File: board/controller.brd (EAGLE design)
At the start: 100 x 100 mm, 61 parts, among them J1 X, J10 COOLANT, J12 VIN, J13 GND, J15 A, J16 +5V, J17 PROBE, J18 FEED_OVERRIDE, J19 MOTOR_CURRENT, J2 Y, J20 WHEEL, J22 DISPLAY, J23 ERROR, J24 HOLDING, J25 SPINDLE, J26 SD_READER, J3 Z, J4 RESET, J5 Z_DISPLAY, J6 FEED_HOLD, J8 CYCLE_START, U5 SENSOR-IR-THRU

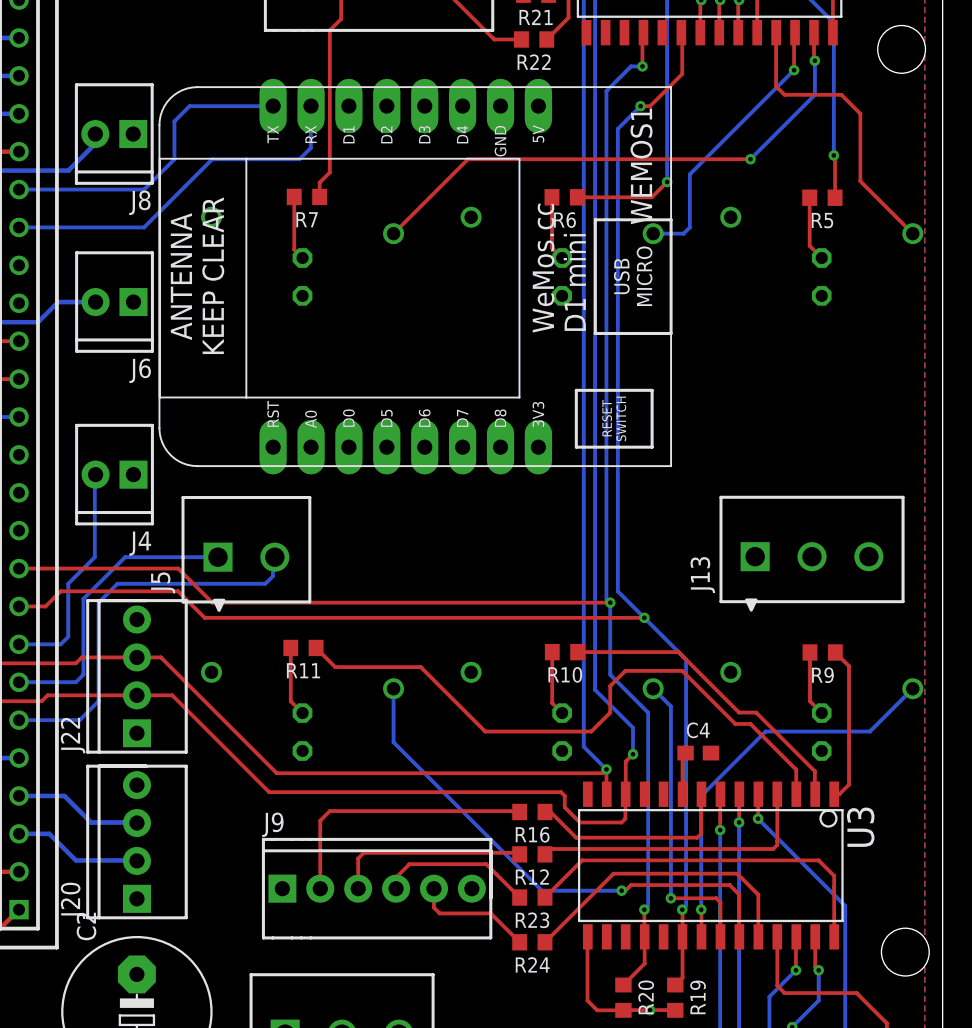
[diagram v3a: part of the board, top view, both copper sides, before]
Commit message: fixed 5V0/GND islands
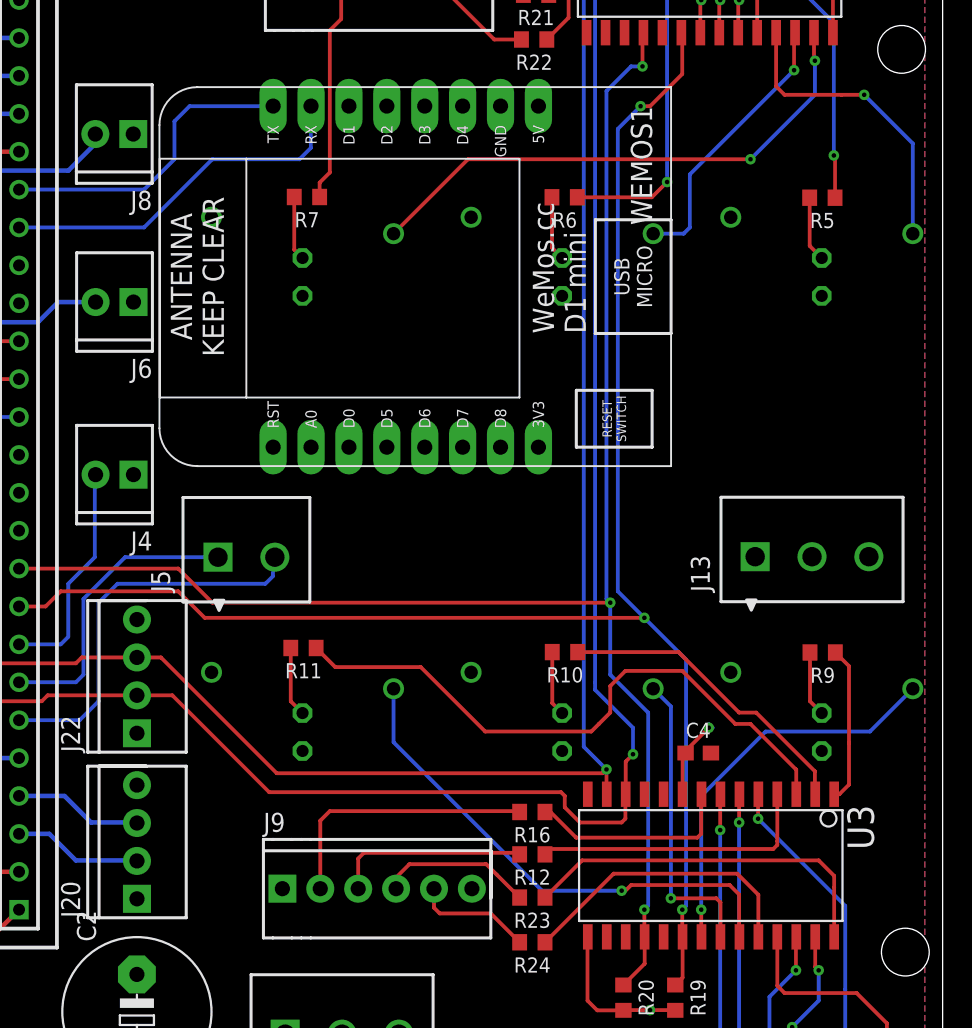
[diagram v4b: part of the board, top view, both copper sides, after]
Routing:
- net 5V0: track 22.3 -> 25.2 mm, vias 3 -> 4
- net S2A1: track 19.5 -> 20.4 mm, vias 0 -> 1
- net RESET_IN: vias 1 -> 0

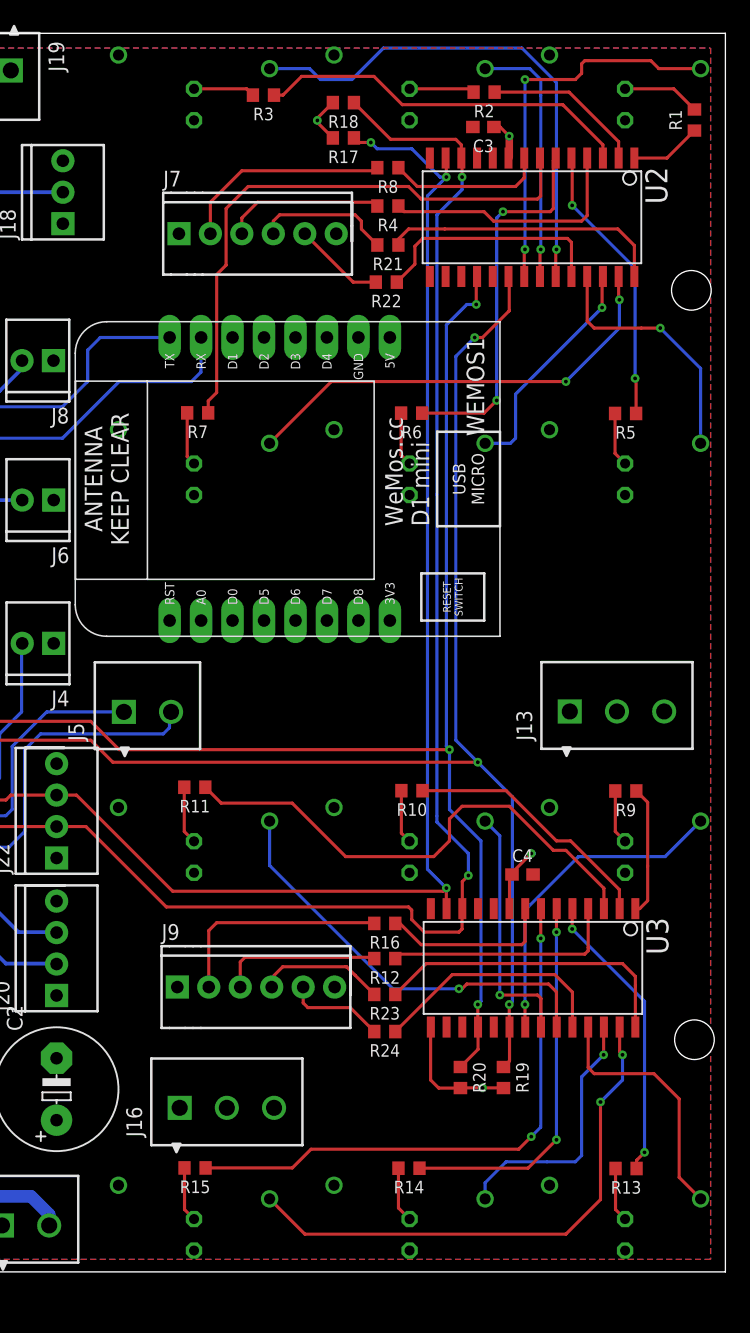
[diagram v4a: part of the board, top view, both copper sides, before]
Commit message: corrected keyboard switch dimensions
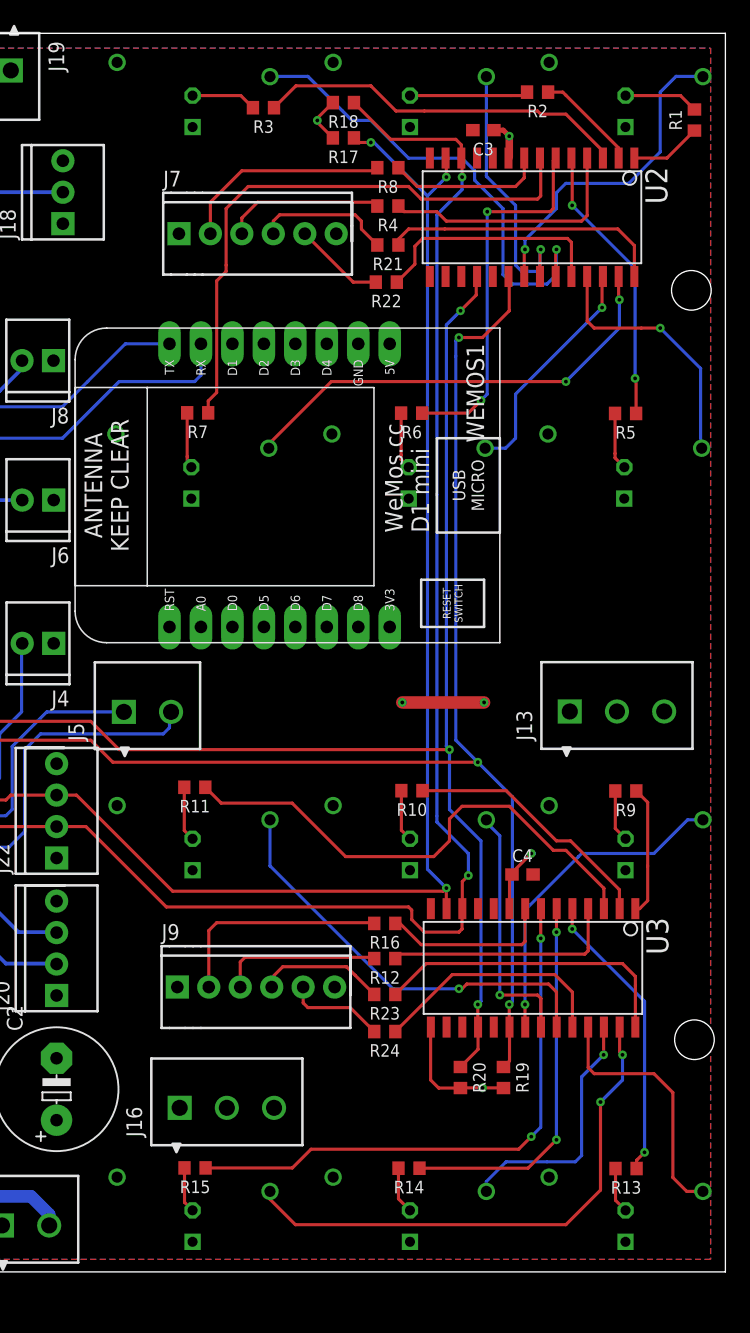
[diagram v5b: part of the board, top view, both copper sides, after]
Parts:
- moved S1 27.7 mm to (100.6, 84.9)
- moved S2 27.5 mm to (100.5, 54.9)
- moved S3 27.5 mm to (100.6, 24.9)
- moved S4 27.3 mm to (100.6, -5.10)
- moved R2 4.32 mm to (84.8, 95.2)
- moved R3 1.02 mm to (62.7, 94.0)
- moved WEMOS1 0.52 mm to (62.7, 62.2)
- moved C3 0.25 mm to (80.5, 92.2)
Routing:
- net 5V0: track 25.2 -> 31.7 mm, vias 4 -> 6
- net S1A1: track 31.4 -> 26.4 mm, vias 2 -> 1
- net N$2: track 13.0 -> 8.37 mm
- net S1BA: track 5.69 -> 9.57 mm
- net S1C1: track 41.4 -> 38.2 mm
- net RADIO_TX: track 20.8 -> 19.1 mm
- net S1B1: track 20.9 -> 22.3 mm
- net I2C_SDA: track 137.3 -> 136.4 mm
- net S4CA: track 4.45 -> 3.69 mm
- net !IO_INT: track 111.3 -> 112.0 mm
- net S4BA: track 4.48 -> 3.79 mm
- net S4AA: track 4.40 -> 3.71 mm
- net S4B1: track 21.1 -> 20.5 mm
- net N$15: track 30.5 -> 30.0 mm

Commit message: finished routing, almost ready to send
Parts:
- removed J25: SPINDLE, holla:CONN-3.81MM-KF2EDG-4
- added C5: 47u, holla:E5-10
- added FID1, FID2: FIDUCIAL1.5X3, holla:FIDUCIAL-1.5X3
- added GND: (no value), holla:TPTHRU
- added J11: SD_READER, holla:1X06
- added J14: GND, holla:CONN-3.81MM-KF2EDG-3
- added J21: (no value), holla:CONN-.100-6
- added R25, R26: (no value), holla:R0603
- C1, C2: device holla:E5-10 -> holla:C0603
- C3: value (none) -> 1u
- C4: value (none) -> 47u; device holla:C0603 -> holla:E5-10
- J1: value X -> COOLANT; device holla:CONN-3.81MM-KF2EDG-4 -> holla:CONN-3.81MM-KF2EDG-2
- J10: value COOLANT -> FEED_HOLD; device holla:CONN-3.81MM-KF2EDG-2 -> holla:CONN-.100-2
- J12: value VIN -> RESET; device holla:CONN-3.81MM-KF2EDG-2 -> holla:CONN-.100-2
- J13: value GND -> Z; device holla:CONN-3.81MM-KF2EDG-3 -> holla:CONN-3.81MM-KF2EDG-4
- J15: value A -> Z_DISPLAY; device holla:CONN-3.81MM-KF2EDG-4 -> holla:CONN-3.81MM-KF2EDG-2
- J16: value +5V -> (none); device holla:CONN-3.81MM-KF2EDG-3 -> holla:CONN-.100-5
- J17: value PROBE -> (none); device holla:CONN-3.81MM-KF2EDG-3 -> holla:1X02
- J18: value FEED_OVERRIDE -> DISPLAY; device holla:CONN-.100-3 -> holla:CONN-.100-4
- J19: value MOTOR_CURRENT -> A; device holla:CONN-3.81MM-KF2EDG-3 -> holla:CONN-3.81MM-KF2EDG-4
- J2: value Y -> PROBE; device holla:CONN-3.81MM-KF2EDG-4 -> holla:CONN-3.81MM-KF2EDG-3
- J20: value WHEEL -> HOLDING; device holla:CONN-.100-4 -> holla:CONN-.100-2
- J22: value DISPLAY -> WHEEL
- J23: value ERROR -> SPINDLE; device holla:CONN-.100-2 -> holla:CONN-3.81MM-KF2EDG-4
- J24: value HOLDING -> +5V; device holla:CONN-.100-2 -> holla:CONN-3.81MM-KF2EDG-3
- J26: value SD_READER -> GND; device holla:1X06 -> holla:CONN-3.81MM-KF2EDG-3
- J3: value Z -> MOTOR_CURRENT; device holla:CONN-3.81MM-KF2EDG-4 -> holla:CONN-3.81MM-KF2EDG-3
- J4: value RESET -> X; device holla:CONN-.100-2 -> holla:CONN-3.81MM-KF2EDG-4
- J5: value Z_DISPLAY -> (none); device holla:CONN-3.81MM-KF2EDG-2 -> holla:CONN-.100-6
- J6: value FEED_HOLD -> ERROR
- J7: device holla:CONN-.100-6 -> holla:1X05
- J9: value (none) -> Y; device holla:CONN-.100-6 -> holla:CONN-3.81MM-KF2EDG-4
- R17, R18: value 2.2k -> (none)
- R19, R20: value 10k -> (none)
- R2, R5: value (none) -> 2.2k
- R22, R23: value (none) -> 10k
- U1: device holla:BOARD-PSOC-CY8CKIT-059 -> holla:SO28W
- U2: device holla:SO28W -> holla:BOARD-PSOC-CY8CKIT-059
- moved C1 102.8 mm to (80.5, 92.2), turned to 180 degrees
- moved J13 88.4 mm to (3.00, 49.8), turned to 270 degrees
- moved C3 85.1 mm to (21.3, 31.0), turned to 0 degrees
- moved R18 82.9 mm to (21.3, 26.7), turned to 0 degrees
- moved J19 73.6 mm to (3.00, 32.5), turned to 270 degrees
- moved J23 69.1 mm to (3.00, 15.2), turned to 270 degrees
- moved J9 68.7 mm to (3.00, 67.0), turned to 270 degrees
- moved U1 65.4 mm to (85.0, 85.1)
- moved U2 65.4 mm to (27.9, 53.3)
- moved R22 64.5 mm to (78.6, 15.7), turned to 270 degrees
- moved R17 64.0 mm to (72.5, 27.6)
- moved R21 63.5 mm to (72.5, 19.4)
- moved J3 59.1 mm to (38.5, 97.0), turned to 180 degrees
- moved J17 58.8 mm to (13.5, 39.4), turned to 90 degrees
- moved J26 57.3 mm to (43.2, 3.76), turned to 0 degrees
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- renumbered S1 to S103, S2 to S102, S3 to S101, S4 to S100, U5 to U100
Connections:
- removed net N$39: U1.15.4
- new net FEED_OVERRIDE_BTN: J7.5, U2.1.0
- new net FEED_OVERRIDE_OFF: J7.4, U2.1.1
- new net P12.3: J16.4, U2.12.3
- new net P12.4: J16.3, U2.12.4
- new net P12.5: J16.2, U2.12.5
- new net VIN_SCALE: C3.1, R16.2, R18.1, U2.1.4
- net !IO_INT: now also R23.1, U1.20, U2.12.7; no longer R19.1, U1.12.7, U2.20
- net !IO_RESET: now also R22.1, U1.18, U2.12.6; no longer R20.1, U1.12.6, U2.18
- net 5V0: now also C1.1, C2.1, C4.+, J11.1, J16.5, J18.2, J2.3, J21.6, J23.4, J24.1, J24.2, J24.3, J3.3, J5.6, J7.3, R2.2, R22.2, R23.2, R5.2, U1.9, U2.VCC; no longer C2.+, C3.1, C4.1, J16.1, J16.2, J16.3, J17.3, J18.3, J19.3, J20.4, J25.4, J26.1, J7.6, J9.6, R17.2, R18.2, R19.2, R20.2, U1.VCC, U2.9
- net A_DIRECTION_OUT: now also J19.4, U2.0.7; no longer J15.4, U1.0.7
- net A_LIMIT_IN: now also J19.2, U2.0.5; no longer J15.2, U1.0.5
- net A_STEP_OUT: now also J19.3, U2.0.6; no longer J15.3, U1.0.6
- net COOLANT_ENABLE_OUT: now also J1.2, U2.15.4; no longer J10.2, U1.1.4
- net CYCLE_START_IN: now also U2.15.2; no longer U1.15.2
- net ERROR_INDICATOR_OUT: now also J6.2, U2.3.2; no longer J23.2, U1.3.2
- net FEED_HOLDING_OUT: now also J20.2, U2.0.4; no longer J24.2, U1.0.4
- net FEED_HOLD_IN: now also J10.2, U2.15.3; no longer J6.2, U1.15.3
- net FEED_OVERRIDE_IN: now also J7.2, U2.1.7; no longer J18.2, U1.1.7
- net GND: now also C1.2, C2.2, C4.-, C5.-, GND.1, J11.2, J14.1, J14.2, J14.3, J16.1, J21.1, J26.1, J5.1, R16.1, U1.10, U1.15, U1.16, U1.17, U2.GND@1, U2.GND@2, U2.GND@3; no longer C1.-, C2.-, C4.2, J13.2, J13.3, J15.1, J17.1, J24.1, J25.1, J26.2, U1.GND@1, U1.GND@2, U1.GND@3, U2.10, U2.15, U2.16, U2.17
- net I2C_SCL: now also J18.4, R2.1, U1.12, U2.12.0; no longer J22.2, R18.1, U1.12.0, U2.12
- net I2C_SDA: now also J18.3, R5.1, U1.13, U2.12.1; no longer J22.3, R17.1, U1.12.1, U2.13
- net IR_RECEIVE_IN: now also U2.2.4; no longer U1.2.4
- net MOTOR_CURRENT_IN: now also J3.2, U2.1.6; no longer J19.2, U1.1.6
- net N$1: now also R4.1, U1.1; no longer R1.1, U2.1
- net N$10: now also J21.5, R21.2; no longer J9.5, R24.2
- net N$11: now also J21.4, R20.2; no longer J9.4, R23.2
- net N$15: now also U1.3; no longer U2.3
- net N$16: now also R7.1, U1.4; no longer R4.1, U2.4
- net N$17: now also R12.1, U1.5; no longer R5.1, U2.5
- net N$18: now also R11.1, U1.6; no longer R6.1, U2.6
- net N$19: now also R10.1, U1.7; no longer R7.1, U2.7
- net N$2: now also R1.1, U1.2; no longer R2.1, U2.2
- net N$20: now also R6.1, U1.8; no longer R8.1, U2.8
- net N$21: now also R15.1; no longer R9.1
- net N$22: now also R14.1; no longer R10.1
- net N$23: now also R13.1; no longer R11.1
- net N$24: now also R19.1; no longer R12.1
- net N$25: now also R26.1; no longer R13.1
- net N$26: now also R25.1; no longer R14.1
- net N$27: now also R24.1; no longer R15.1
- net N$28: now also R17.1; no longer R16.1
- net N$3: now also R9.1, U1.24; no longer R22.1, U2.24
- net N$30: now also J5.2, R6.2; no longer J7.2, R8.2
- net N$4: now also J5.5, R9.2; no longer J7.5, R22.2
- net N$43: now also J17.2, U2.0.2; no longer U1.0.2
- net N$44: now also J21.3, R19.2; no longer J9.3, R12.2
- net N$45: now also J17.1, U2.0.3; no longer U1.0.3
- net N$48: now also J21.2, R17.2; no longer J9.2, R16.2
- net N$5: now also R8.1, U1.28; no longer R21.1, U2.28
- net N$6: now also J5.3, R7.2; no longer J7.3, R4.2
- net N$7: now also J5.4, R8.2; no longer J7.4, R21.2
- net N$8: now also R21.1; no longer R24.1
- net N$9: now also R20.1; no longer R23.1
- net PROBE_IN: now also J2.2, U2.1.5; no longer J17.2, U1.1.5
- net RADIO_RX: now also U2.1.2; no longer U1.1.2
- net RADIO_TX: now also U2.1.3; no longer U1.1.3
- net RESET_IN: now also J12.2, U2.2.7; no longer J4.2, U1.2.7
- net S1A1: now also U1.21; no longer U2.21
- net S1AA: now also R4.2; no longer R1.2
- net S1B1: now also U1.22; no longer U2.22
- net S1BA: now also R1.2; no longer R2.2
- net S1C1: now also U1.23; no longer U2.23
- net S2A1: now also U1.25; no longer U2.25
- net S2AA: now also R12.2; no longer R5.2
- net S2B1: now also U1.26; no longer U2.26
- net S2BA: now also R11.2; no longer R6.2
- net S2C1: now also U1.27; no longer U2.27
- net S2CA: now also R10.2; no longer R7.2
- net S3AA: now also R15.2; no longer R9.2
- net S3BA: now also R14.2; no longer R10.2
- net S3CA: now also R13.2; no longer R11.2
- net S4AA: now also R26.2; no longer R13.2
- net S4BA: now also R25.2; no longer R14.2
- net S4CA: now also R24.2; no longer R15.2
- net SD_READER_CS: now also J11.4, U2.15.1; no longer J26.4, U1.15.1
- net SPINDLE_DIRECTION_OUT: now also J23.3, U2.2.0; no longer J25.3, U1.2.0
- net SPINDLE_ENABLE_OUT: now also J23.2, U2.2.1; no longer J25.2, U1.2.1
- net SPI_MISO: now also J11.6, U2.3.7; no longer J26.6, U1.3.7
- net SPI_MOSI: now also J11.3, U2.12.2; no longer J26.3, U1.12.2
- net SPI_SCK: now also J11.5, U2.15.0; no longer J26.5, U1.15.0
- net VIN: now also C5.+, J26.2, J26.3, R18.2; no longer C1.+, J12.2
- net WHEEL_ENCODER_A_IN: now also J22.3, U2.2.3; no longer J20.3, U1.2.3
- net WHEEL_ENCODER_B_IN: now also J22.2, U2.2.2; no longer J20.2, U1.2.2
- net X_DIRECTION_OUT: now also J4.4, U2.3.3; no longer J1.4, U1.3.3
- net X_LIMIT_IN: now also J4.2, U2.3.0; no longer J1.2, U1.3.0
- net X_STEP_OUT: now also J4.3, U2.3.1; no longer J1.3, U1.3.1
- net Y_DIRECTION_OUT: now also J9.4, U2.3.6; no longer J2.4, U1.3.6
- net Y_LIMIT_IN: now also J9.2, U2.3.4; no longer J2.2, U1.3.4
- net Y_STEP_OUT: now also J9.3, U2.3.5; no longer J2.3, U1.3.5
- net Z_DIRECTION_OUT: now also J13.4, U2.0.1; no longer J3.4, U1.0.1
- net Z_DISPLAY_RX_IN: now also J15.2, U2.2.5; no longer J5.2, U1.2.5
- net Z_DISPLAY_TX_OUT: now also J15.1, U2.2.6; no longer J5.1, U1.2.6
- net Z_LIMIT_IN: now also J13.2, U2.15.5; no longer J3.2, U1.15.5
- net Z_STEP_OUT: now also J13.3, U2.0.0; no longer J3.3, U1.0.0
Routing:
- net VIN_SCALE: track 0.00 -> 61.9 mm, vias 0 -> 1
- net P12.3: track 0.00 -> 35.5 mm
- net VIN: track 36.6 -> 69.0 mm
- net P12.4: track 0.00 -> 31.0 mm
- net FEED_OVERRIDE_BTN: track 0.00 -> 29.5 mm
- net P12.5: track 0.00 -> 27.3 mm
- net FEED_OVERRIDE_OFF: track 0.00 -> 25.9 mm
- net I2C_SCL: track 151.4 -> 165.4 mm, vias 2 -> 3
- net FEED_OVERRIDE_IN: track 20.8 -> 8.44 mm
- net RESET_IN: track 15.1 -> 24.4 mm
- net COOLANT_ENABLE_OUT: track 45.1 -> 53.4 mm, vias 0 -> 1
- net Y_STEP_OUT: track 16.7 -> 24.5 mm
- net S3A1: track 26.8 -> 33.1 mm
- net 5V0: track 31.7 -> 25.8 mm, vias 6 -> 5
- net Y_LIMIT_IN: track 16.2 -> 22.0 mm
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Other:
- board text added: "+"
- board text added: "-"
- board text added: "5V0"
- board text added: "A"
- board text added: "COOLANT"
- board text added: "CYCLE START"
- board text added: "ERROR"
- board text added: "FEED HOLD"
- board text added: "FEED OVERRIDE"
- board text added: "GND"
- board text added: "HOLDING"
- board text added: "Hyatt CNC Controller 180804 v1.0 ValveStudio"
- board text added: "I/O CPU"
- board text added: "I/O SPARE 1"
- board text added: "I/O SPARE 2"
- board text added: "I2C DISP"
- board text added: "MOTOR CURRENT"
- board text added: "PROBE"
- board text added: "RESET"
- board text added: "SD CARD/SPI"
- board text added: "SPINDLE"
- board text added: "VIN"
- board text added: "WHEEL"
- board text added: "X"
- board text added: "Y"
- board text added: "Z"
- board text added: "Z DISP"
